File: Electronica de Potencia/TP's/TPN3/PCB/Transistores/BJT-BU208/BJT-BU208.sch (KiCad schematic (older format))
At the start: 20 parts

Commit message: Avanzo el tp3 de potencia
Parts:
- added JP?: Jumper_NC_Small, symbol Device:Jumper_NC_Small
- added JP?: Jumper_NC_Dual, symbol Device:Jumper_NC_Dual
- Q?: value BC368 -> BC548
- Q?: value BC369 -> BC558
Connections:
- net at D?.2 (A), D?.2 (A): now also JP?.1; no longer Q?.3 (E)
- net at Q?.1 (C), R?.2: now also JP?.2; no longer D?.1 (K)
- net at D?.1 (K), Q?.1 (C), Q?.2 (B): now also JP?.3
- new net: D?.1 (K), JP?.1
- new net: JP?.2, Q?.3 (E)
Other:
- moved on the sheet: D?, Q?, R?
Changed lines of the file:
@@
 EESchema Schematic File Version 4
+LIBS:BJT-BU208-cache
 EELAYER 29 0
 EELAYER END
@@
 P 5200 3650
 F 0 "Q?" H 5391 3696 50  0000 L CNN
-F 1 "BC368" H 5391 3605 50  0000 L CNN
+F 1 "BC548" H 5391 3605 50  0000 L CNN
 F 2 "Package_TO_SOT_THT:TO-92_Inline" H 5400 3575 50  0001 L CIN
 F 3 "https://diotec.com/tl_files/diotec/files/pdf/datasheets/bc337.pdf" H 5200 3650 50  0001 L CNN
@@
 L Diode:1N4148 D?
 U 1 1 5CDA9EFD
-P 5750 4600
-F 0 "D?" H 5750 4500 50  0000 C CNN
-F 1 "MUR160" H 5750 4700 50  0000 C CNN
-F 2 "Diode_THT:D_DO-35_SOD27_P7.62mm_Horizontal" H 5750 4425 50  0001 C CNN
-F 3 "https://assets.nexperia.com/documents/data-sheet/1N4148_1N4448.pdf" H 5750 4600 50  0001 C CNN
-	1    5750 4600
+P 5850 4600
+F 0 "D?" H 5850 4500 50  0000 C CNN
+F 1 "MUR160" H 5850 4700 50  0000 C CNN
+F 2 "Diode_THT:D_DO-35_SOD27_P7.62mm_Horizontal" H 5850 4425 50  0001 C CNN
+F 3 "https://assets.nexperia.com/documents/data-sheet/1N4148_1N4448.pdf" H 5850 4600 50  0001 C CNN
+	1    5850 4600
 	-1   0    0    1
 $EndComp
 Wire Wire Line
-	5600 4600 5300 4600
+	5700 4600 5600 4600
 $Comp
 L Diode:1N4148 D?
 U 1 1 5CDAD3F1
-P 6300 4600
-F 0 "D?" H 6300 4500 50  0000 C CNN
-F 1 "MUR160" H 6300 4700 50  0000 C CNN
-F 2 "Diode_THT:D_DO-35_SOD27_P7.62mm_Horizontal" H 6300 4425 50  0001 C CNN
-F 3 "https://assets.nexperia.com/documents/data-sheet/1N4148_1N4448.pdf" H 6300 4600 50  0001 C CNN
-	1    6300 4600
+P 6200 4600
+F 0 "D?" H 6200 4500 50  0000 C CNN
+F 1 "MUR160" H 6200 4700 50  0000 C CNN
+F 2 "Diode_THT:D_DO-35_SOD27_P7.62mm_Horizontal" H 6200 4425 50  0001 C CNN
+F 3 "https://assets.nexperia.com/documents/data-sheet/1N4148_1N4448.pdf" H 6200 4600 50  0001 C CNN
+	1    6200 4600
 	-1   0    0    1
 $EndComp
 Wire Wire Line
-	6150 4600 5900 4600
+	6050 4600 6000 4600
 $Comp
 L Diode:1N4148 D?
 U 1 1 5CDAF349
-P 5300 4950
-F 0 "D?" V 5346 4871 50  0000 R CNN
-F 1 "1N4148" V 5255 4871 50  0000 R CNN
-F 2 "Diode_THT:D_DO-35_SOD27_P7.62mm_Horizontal" H 5300 4775 50  0001 C CNN
-F 3 "https://assets.nexperia.com/documents/data-sheet/1N4148_1N4448.pdf" H 5300 4950 50  0001 C CNN
-	1    5300 4950
+P 5600 5100
+F 0 "D?" V 5646 5021 50  0000 R CNN
+F 1 "1N4148" V 5555 5021 50  0000 R CNN
+F 2 "Diode_THT:D_DO-35_SOD27_P7.62mm_Horizontal" H 5600 4925 50  0001 C CNN
+F 3 "https://assets.nexperia.com/documents/data-sheet/1N4148_1N4448.pdf" H 5600 5100 50  0001 C CNN
+	1    5600 5100
 	0    -1   -1   0
 $EndComp
 Wire Wire Line
-	5300 4800 5300 4600
+	5600 4950 5600 4600
 $Comp
 L Transistor_BJT:BC328 Q?
 U 1 1 5CDB563C
-P 5200 5800
-F 0 "Q?" H 5391 5846 50  0000 L CNN
-F 1 "BC369" H 5391 5755 50  0000 L CNN
-F 2 "Package_TO_SOT_THT:TO-92_Inline" H 5400 5725 50  0001 L CIN
-F 3 "http://www.redrok.com/PNP_BC327_-45V_-800mA_0.625W_Hfe100_TO-92.pdf" H 5200 5800 50  0001 L CNN
-	1    5200 5800
+P 5500 5800
+F 0 "Q?" H 5691 5846 50  0000 L CNN
+F 1 "BC558" H 5691 5755 50  0000 L CNN
+F 2 "Package_TO_SOT_THT:TO-92_Inline" H 5700 5725 50  0001 L CIN
+F 3 "http://www.redrok.com/PNP_BC327_-45V_-800mA_0.625W_Hfe100_TO-92.pdf" H 5500 5800 50  0001 L CNN
+	1    5500 5800
 	1    0    0    -1
 $EndComp
@@
 L power:-5V #PWR?
 U 1 1 5CDB79B3
-P 5300 6100
-F 0 "#PWR?" H 5300 6200 50  0001 C CNN
-F 1 "-5V" H 5315 6273 50  0000 C CNN
-F 2 "" H 5300 6100 50  0001 C CNN
-F 3 "" H 5300 6100 50  0001 C CNN
-	1    5300 6100
+P 5600 6150
+F 0 "#PWR?" H 5600 6250 50  0001 C CNN
+F 1 "-5V" H 5615 6323 50  0000 C CNN
+F 2 "" H 5600 6150 50  0001 C CNN
+F 3 "" H 5600 6150 50  0001 C CNN
+	1    5600 6150
 	-1   0    0    1
 $EndComp
 Wire Wire Line
-	5300 6100 5300 6050
+	5600 6150 5600 6050
 $Comp
 L Device:R_US R?
 U 1 1 5CDB991D
-P 4950 6050
-F 0 "R?" V 4850 6050 50  0000 C CNN
-F 1 "1k" V 5050 6050 50  0000 C CNN
-F 2 "" V 4990 6040 50  0001 C CNN
-F 3 "~" H 4950 6050 50  0001 C CNN
-	1    4950 6050
+P 5150 6050
+F 0 "R?" V 5050 6050 50  0000 C CNN
+F 1 "1k" V 5250 6050 50  0000 C CNN
+F 2 "" V 5190 6040 50  0001 C CNN
+F 3 "~" H 5150 6050 50  0001 C CNN
+	1    5150 6050
 	0    1    1    0
 $EndComp
 Wire Wire Line
-	5100 6050 5300 6050
-Connection ~ 5300 6050
-Wire Wire Line
-	5300 6050 5300 6000
-Wire Wire Line
-	4800 6050 4700 6050
+	5300 6050 5600 6050
+Connection ~ 5600 6050
+Wire Wire Line
+	5600 6050 5600 6000
+Wire Wire Line
+	5000 6050 4700 6050
 Wire Wire Line
 	4700 6050 4700 5800
@@
 	4700 3650 5000 3650
 Wire Wire Line
-	5000 5800 4700 5800
+	5300 5800 4700 5800
 Connection ~ 4700 5800
 $Comp
@@
 	1    0    0    -1
 $EndComp
-Wire Wire Line
-	6700 5250 6700 4600
-Wire Wire Line
-	6700 4600 6450 4600
 $Comp
 L power:GND #PWR?
@@
 	1    0    0    -1
 $EndComp
-Connection ~ 6700 4600
 $Comp
 L power:+15V #PWR?
@@
 Text Notes 5250 3200 1    50   ~ 0
 3W
-Connection ~ 5300 4600
-Wire Wire Line
-	6400 5450 5300 5450
-Connection ~ 5300 5450
-Wire Wire Line
-	5300 5450 5300 5600
+Wire Wire Line
+	6400 5450 5600 5450
+Connection ~ 5600 5450
+Wire Wire Line
+	5600 5450 5600 5600
+Wire Wire Line
+	5600 5250 5600 5450
+$Comp
+L Device:Jumper_NC_Small JP?
+U 1 1 5CD9CA06
+P 6450 4600
+F 0 "JP?" H 6450 4721 50  0000 C CNN
+F 1 "Jumper_NC_Small" H 6450 4721 50  0001 C CNN
+F 2 "" H 6450 4600 50  0001 C CNN
+F 3 "~" H 6450 4600 50  0001 C CNN
+	1    6450 4600
+	1    0    0    -1
+$EndComp
 Wire Wire Line
 	6700 3300 6700 4600
 Wire Wire Line
-	5300 3850 5300 4600
-Wire Wire Line
-	5300 5100 5300 5450
+	6700 4600 6550 4600
+Connection ~ 6700 4600
+Wire Wire Line
+	6700 4600 6700 5250
+$Comp
+L Device:Jumper_NC_Dual JP?
+U 1 1 5CDA481A
+P 5300 4150
+F 0 "JP?" H 5300 4297 50  0000 C CNN
+F 1 "Jumper_NC_Dual" H 5300 4388 50  0001 C CNN
+F 2 "" H 5300 4150 50  0001 C CNN
+F 3 "~" H 5300 4150 50  0001 C CNN
+	1    5300 4150
+	-1   0    0    1
+$EndComp
+Wire Wire Line
+	5300 4050 5300 3850
+Wire Wire Line
+	5550 4150 5600 4150
+Wire Wire Line
+	5600 4150 5600 4600
+Connection ~ 5600 4600
+Wire Wire Line
+	4950 4150 4950 5450
+Wire Wire Line
+	4950 5450 5600 5450
+Wire Wire Line
+	4950 4150 5050 4150
 $EndSCHEMATC

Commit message: Actualizo con placa 2 de potencia
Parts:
- added TP1: TP_Base, lib_fp:Testpoint, symbol BJT-BU208:TestPoint_Probe
- added TP2: TP_Colector, lib_fp:Testpoint, symbol BJT-BU208:TestPoint_Probe
- added TP3: GND, lib_fp:Testpoint, symbol BJT-BU208:TestPoint_Probe
- C1: renamed from C?; footprint (none) -> lib_fp:C_Disc_D4.7mm_W2.5mm_P5.00mm; symbol Device:CP1 -> BJT-BU208:CP1
- C2, C4: renamed from C?; footprint (none) -> lib_fp:C_Radial_D5.0mm_H11.0mm_P2.00mm; symbol Device:CP1 -> BJT-BU208:CP1
- C3: renamed from C?; footprint (none) -> lib_fp:C_Disc_D5.0mm_W2.5mm_P2.50mm; symbol Device:CP1 -> BJT-BU208:CP1
- D1: renamed from D?; footprint Diode_THT:D_DO-35_SOD27_P7.62mm_Horizontal -> lib_fp:D_DO-34_SOD68_P7.62mm_Horizontal; symbol Diode:1N4148 -> BJT-BU208:1N4148
- D2, D3: renamed from D?; footprint Diode_THT:D_DO-35_SOD27_P7.62mm_Horizontal -> lib_fp:D_DO-41_SOD81_P10.16mm_Horizontal; symbol Diode:1N4148 -> BJT-BU208:1N4148
- HS1, HS2: renamed from HS?; footprint (none) -> lib_fp:Heatsink_TO220_A; symbol Mechanical:Heatsink -> BJT-BU208:Heatsink
- J1, J2: renamed from J?; footprint (none) -> lib_fp:TerminalBlock_bornier-2_P5.08mm; symbol Connector:Screw_Terminal_01x02 -> BJT-BU208:Screw_Terminal_01x02
- JP1: renamed from JP?; footprint (none) -> lib_fp:PinHeader_1x03_P2.54mm_Vertical; symbol Device:Jumper_NC_Dual -> BJT-BU208:Jumper_NC_Dual
- JP2: renamed from JP?; footprint (none) -> lib_fp:PinHeader_1x02_P2.54mm_Vertical; symbol Device:Jumper_NC_Small -> BJT-BU208:Jumper_NC_Small
- Q1: renamed from Q?; footprint Package_TO_SOT_THT:TO-92_Inline -> lib_fp:TO-92_Inline; symbol Transistor_BJT:BC337 -> BJT-BU208:BC337
- Q2: renamed from Q?; footprint Package_TO_SOT_THT:TO-92_Inline -> lib_fp:TO-92_Inline; symbol Transistor_BJT:BC328 -> BJT-BU208:BC328
- Q3: renamed from Q?; footprint Package_TO_SOT_THT:TO-92_Inline -> lib_fp:TO-3; symbol Transistor_BJT:BC337 -> BJT-BU208:BC337
- R1, R2: renamed from R?; footprint (none) -> lib_fp:R_Axial_DIN0207_L6.3mm_D2.5mm_P10.16mm_Horizontal; symbol Device:R_US -> BJT-BU208:R_US
- R3: renamed from R?; footprint (none) -> lib_fp:R_Axial_DIN0516_L15.5mm_D5.0mm_P20.32mm_Horizontal; symbol Device:R_US -> BJT-BU208:R_US
- R4: renamed from R?; footprint (none) -> lib_fp:R_Axial_Power_L48.0mm_W12.5mm_P55.88mm; symbol Device:R_US -> BJT-BU208:R_US
- U1: renamed from U?; footprint (none) -> lib_fp:TO-220-3_Vertical; symbol Regulator_Linear:L7812 -> BJT-BU208:L7812
- U2: renamed from U?; footprint (none) -> lib_fp:TO-220-3_Vertical; symbol Regulator_Linear:L7905 -> BJT-BU208:L7905
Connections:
- net GND: now also TP3.1
- net at JP2.2, Q3.1 (C), R4.2: now also TP2.1
- net at D1.1 (K), JP1.3, Q2.1 (C)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: now also TP1.1
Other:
- moved on the sheet: C1, C2, C3, C4, D1, D2, D3, HS1, HS2, J1, J2, JP1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

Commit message: 22
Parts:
- added G1: logo, lib_fp:logo_utn_fsilk_small, symbol BJT-BU208:logo
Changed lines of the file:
@@
 Wire Wire Line
 	7500 5500 7500 5075
+$Comp
+L BJT-BU208:logo G1
+U 1 1 5CDEF98D
+P 9100 2400
+F 0 "G1" H 9100 2370 60  0001 C CNN
+F 1 "logo" H 9100 2430 60  0001 C CNN
+F 2 "lib_fp:logo_utn_fsilk_small" H 9100 2400 50  0001 C CNN
+F 3 "" H 9100 2400 50  0001 C CNN
+	1    9100 2400
+	1    0    0    -1
+$EndComp
 $EndSCHEMATC

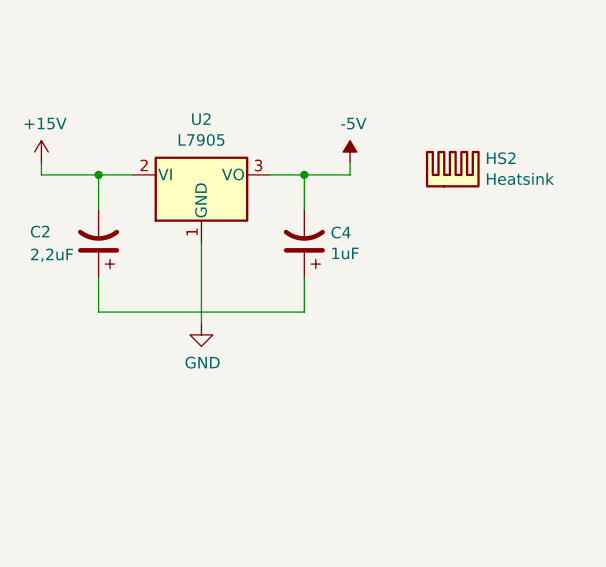
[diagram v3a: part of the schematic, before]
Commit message: Placa TP3 transistor completa
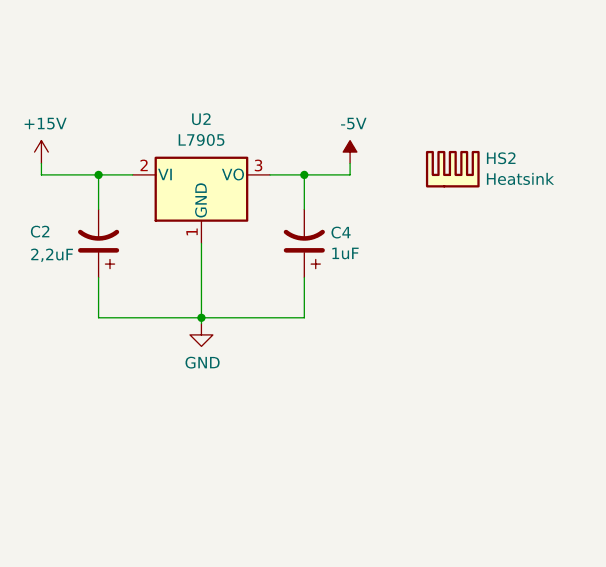
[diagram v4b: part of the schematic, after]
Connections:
- net GND: now also C2.1, C4.1
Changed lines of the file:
@@
 	3250 4125 3400 4125
 Wire Wire Line
-	3250 4725 3250 4575
-Wire Wire Line
 	4150 4275 4150 4125
 Wire Wire Line
 	4150 4125 4000 4125
-Wire Wire Line
-	4150 4575 4150 4725
 Wire Wire Line
 	4350 4075 4350 4125
@@
 	4350 4125 4150 4125
 Connection ~ 4150 4125
-Wire Wire Line
-	3250 4725 4150 4725
 $Comp
 L BJT-BU208:GND #PWR04
@@
 $EndComp
 Wire Wire Line
-	3700 4775 3700 4425
+	3700 4775 3700 4750
 $Comp
 L BJT-BU208:CP1 C1
@@
 	1    0    0    -1
 $EndComp
+Wire Wire Line
+	4150 4575 4150 4750
+Wire Wire Line
+	4150 4750 3700 4750
+Connection ~ 3700 4750
+Wire Wire Line
+	3700 4750 3700 4425
+Wire Wire Line
+	3700 4750 3250 4750
+Wire Wire Line
+	3250 4750 3250 4575
 $EndSCHEMATC
